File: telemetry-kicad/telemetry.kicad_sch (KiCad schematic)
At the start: 50 parts, among them J1 USB_C_Receptacle_USB2.0_16P, Q2 DMP3099LQ-7, SW1 SW_NRST, SW2 SW_BOOT0, U1 STM32H523RCT7, U2 AP2112K-3.3, U3 MAX-M10S-00B, U4 ASM330LHHXG1TR, U5 TCAN1044VDRQ1, U6 LMR33630ADDA, U7 USBLC6-2SC6, U8 TPS2116DRL

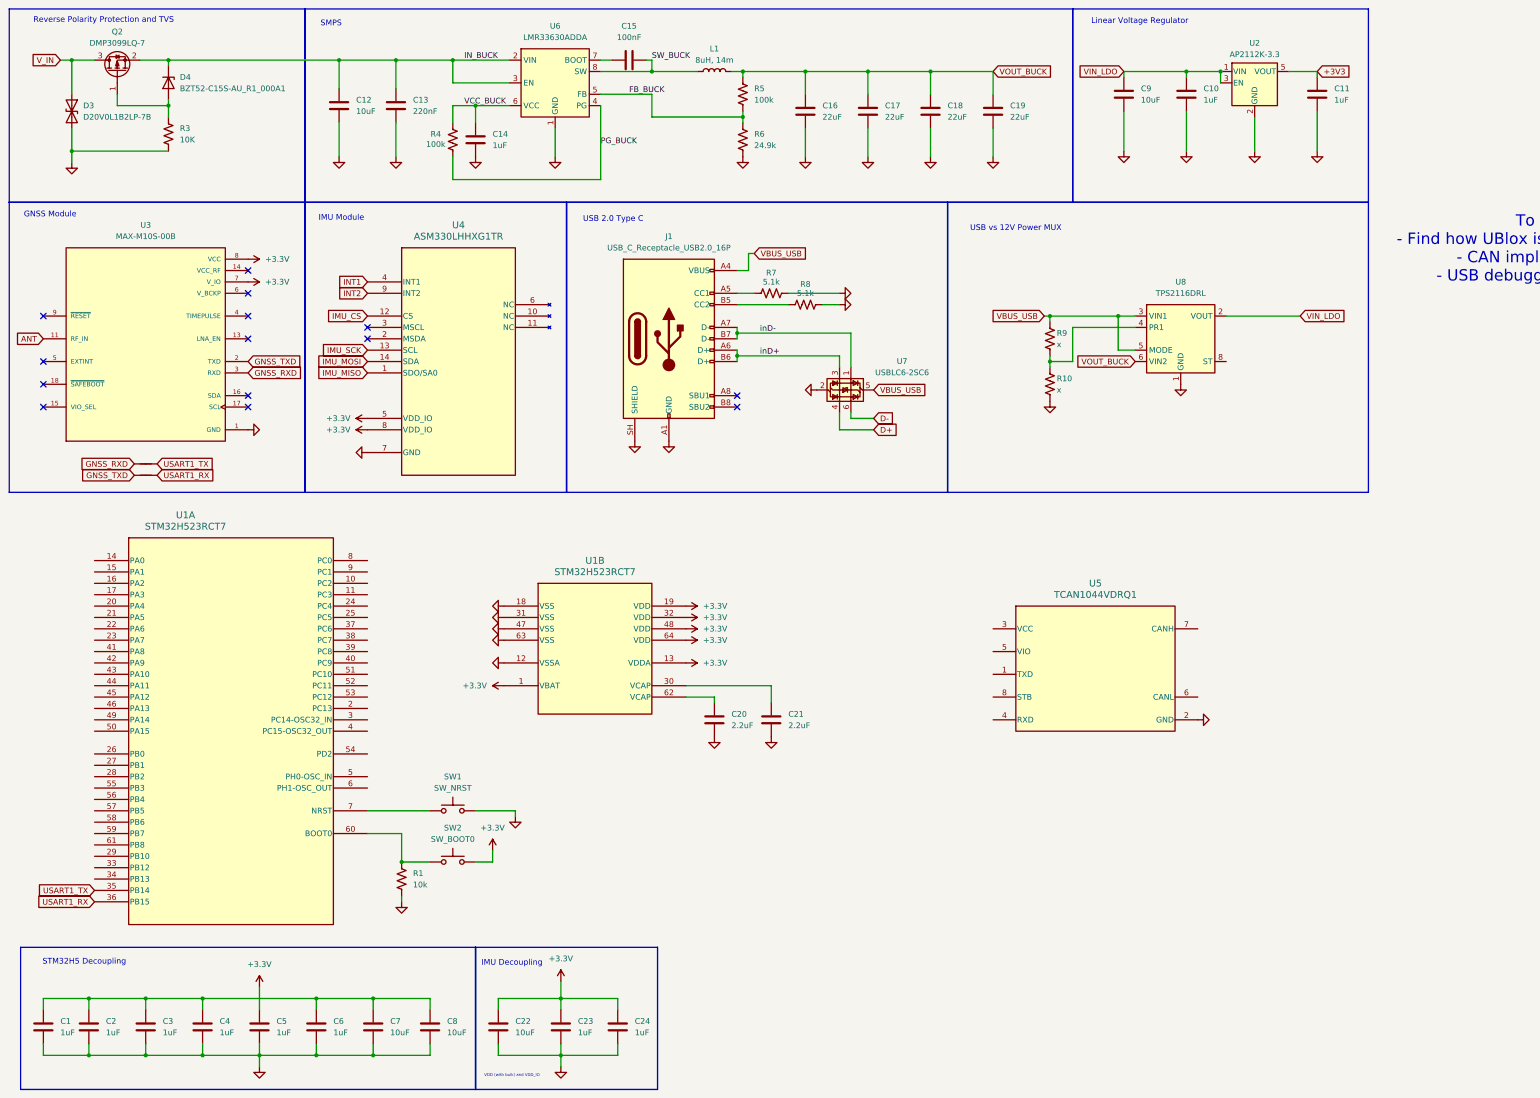
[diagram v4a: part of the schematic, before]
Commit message: Added flash and improved from suggestions. Power status flags go into MCU. Need to work on MCU Pin Plan and update documentation
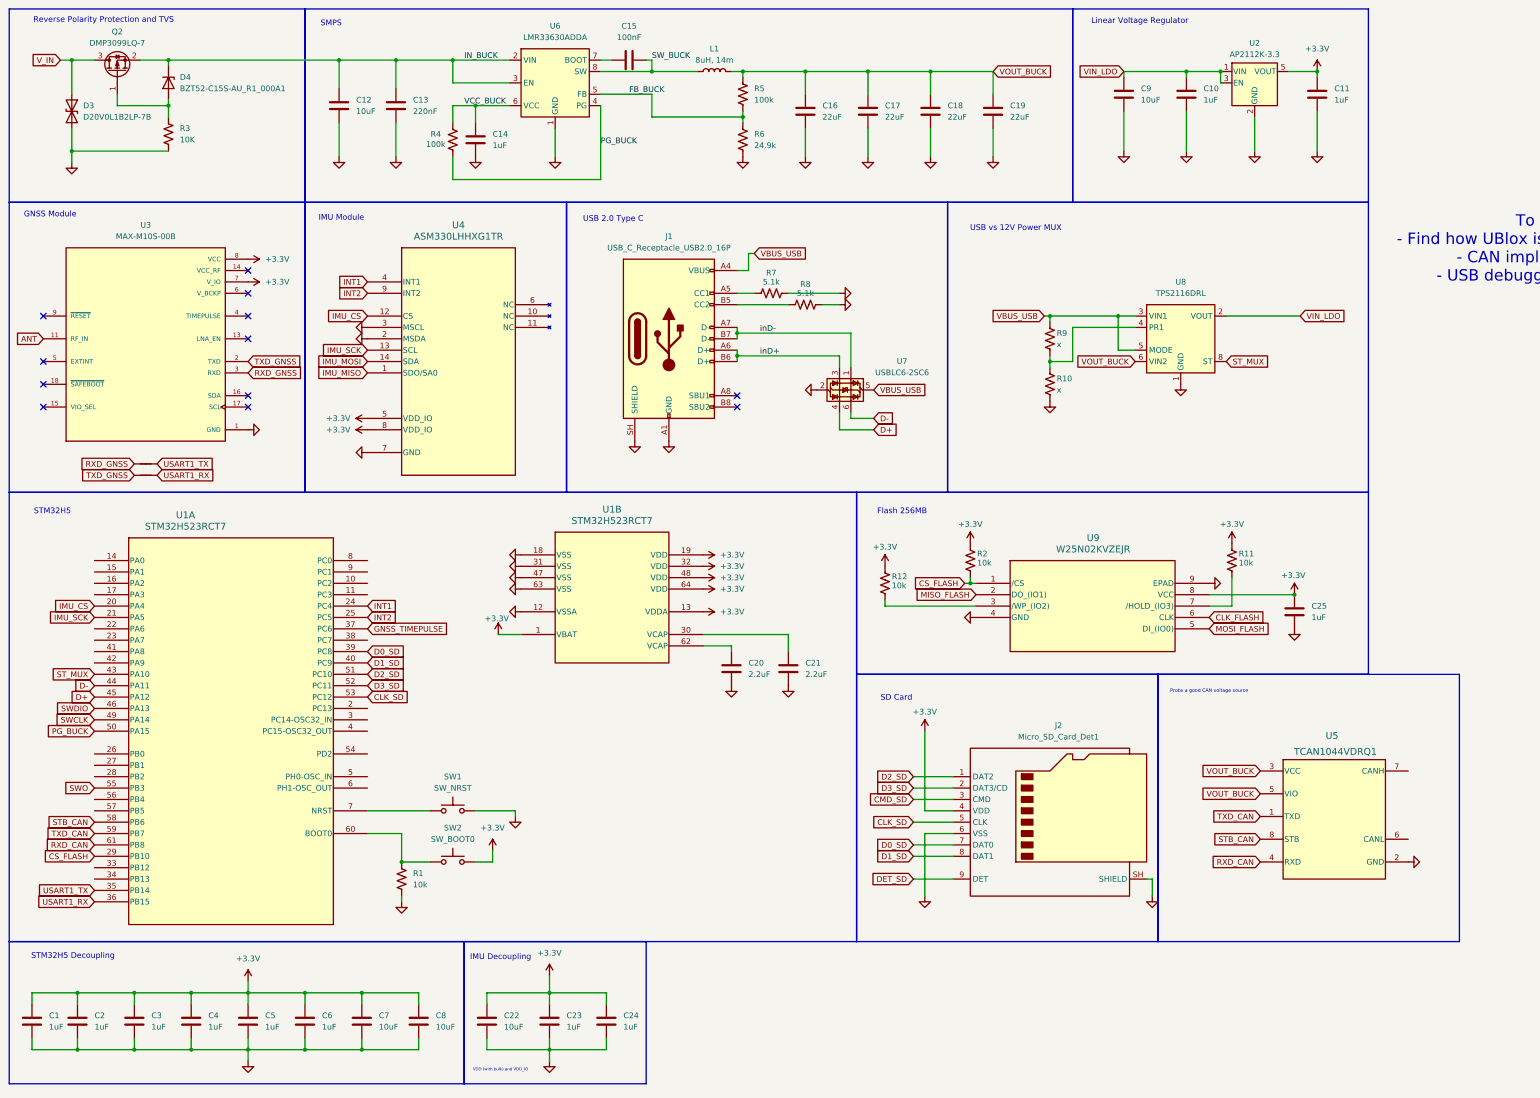
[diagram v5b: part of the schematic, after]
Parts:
- added C25: 1uF, symbol Device:C
- added J2: Micro_SD_Card_Det1, symbol Connector:Micro_SD_Card_Det1
- added R11, R12, R2: 10k, symbol Device:R_US
- added U9: W25N02KVZEJR, u-blox:W25N02KVZEJR, symbol telemetry:W25N02KVZEIR
- U5: footprint (none) -> D0008A-IPC_A
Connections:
- net +3V3 is gone; now on net +3.3V: C11.1, U2.5 (VOUT)
- net +3.3V: now also C1.1, C2.1, C3.1, C4.1, C6.1, C7.1, C8.1, C25.1, J2.4 (VDD), R11.1, R12.1, R2.1, U9.8 (VCC)
- net D+: now also U1.45 (PA12)
- net D-: now also U1.44 (PA11)
- net GND: now also U4.2 (MSDA), U4.3 (MSCL), C25.2, J2.6 (VSS), J2.SH (SHIELD), U9.4 (GND), U9.9 (EPAD)
- net IMU_CS: now also U1.20 (PA4)
- net IMU_SCK: now also U1.21 (PA5)
- net INT1: now also U1.24 (PC4)
- net INT2: now also U1.25 (PC5)
- net PG_BUCK: now also U1.50 (PA15)
- net VOUT_BUCK: now also U5.3 (VCC), U5.5 (VIO)
- net ST_MUX: now reaches U8.8 (ST)
- net ST_MUX: now also U1.43 (PA10)
- net CS_FLASH: now reaches U1.29 (PB10)
- net CS_FLASH: now also R2.2, U9.1 (/CS)
- net GNSS_TIMEPULSE: now reaches U1.37 (PC6)
- net D0_SD: now reaches U1.39 (PC8)
- net D0_SD: now also J2.7 (DAT0)
- net D1_SD: now reaches U1.40 (PC9)
- net D1_SD: now also J2.8 (DAT1)
- net SWDIO: now reaches U1.46 (PA13)
- net SWCLK: now reaches U1.49 (PA14)
- net D2_SD: now reaches U1.51 (PC10)
- net D2_SD: now also J2.1 (DAT2)
- net D3_SD: now reaches U1.52 (PC11)
- net D3_SD: now also J2.2 (DAT3/CD)
- net CLK_SD: now reaches U1.53 (PC12)
- net CLK_SD: now also J2.5 (CLK)
- net SWO: now reaches U1.55 (PB3)
- net STB_CAN: now reaches U1.58 (PB6)
- net STB_CAN: now also U5.8 (STB)
- net TXD_CAN: now reaches U1.59 (PB7)
- net TXD_CAN: now also U5.1 (TXD)
- net RXD_CAN: now reaches U1.61 (PB8)
- net RXD_CAN: now also U5.4 (RXD)
- net GNSS_RXD renamed RXD_GNSS
- net GNSS_TXD renamed TXD_GNSS
- new net: R12.2, U9.3 (/WP_(IO2))
- new net: R11.2, U9.7 (/HOLD_(IO3))
- new net CLK_FLASH: U9.6 (CLK)
- new net CMD_SD: J2.3 (CMD)
- new net DET_SD: J2.9 (DET)
- new net MISO_FLASH: U9.2 (DO_(IO1))
- new net MOSI_FLASH: U9.5 (DI_(IO0))
- no-connect marks 14 -> 12
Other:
- note added: "Flash 256MB"
- note added: "Probs a good CAN voltage source"
- note added: "SD Card"
- note added: "STM32H5"
- moved on the sheet: C1, C2, C20, C21, C22, C23, C24, C3, C4, C5, C6, C7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

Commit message: touch ups
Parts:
- removed C19: 22uF, Capacitor_SMD:C_0805_2012Metric_Pad1.18x1.45mm_HandSolder, symbol Device:C
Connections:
- net VOUT_BUCK is gone; now on net VIN_LDO: C16.1, C17.1, C18.1, L1.2, R5.1, U5.3 (VCC), U5.5 (VIO), U8.6 (VIN2)
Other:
- note added: "Fix net names"
- note added: "To do: - Find how UBlox is layed out on PCB - CAN terminal block - SMA connector for UBlox - HSE Crystal"
- note removed: "Probs a good CAN voltage source"
- note removed: "To do: - Find how UBlox is layed out on PCB - CAN implimentation - USB debugging and SWD"
- moved on the sheet: C10, C9

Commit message: Schematic wiring, CAN terminal block added and SMA connector added
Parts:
- added J3: 2601-1102, CONN2_2601-1102_WAG, symbol telemetry:2601-1102
- added J4: RFPC-SMA27-F, RFPC-SMA27-F:GRADCONN_RFPC-SMA27-F, symbol telemetry:RFPC-SMA27-F
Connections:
- net GNSS_TIMEPULSE is gone; now on net TIMEPULSE_GNSS: U1.37 (PC6)
- net IMU_MISO is gone; now on net MISO_IMU: U4.1 (SDO/SA0)
- net IMU_MOSI is gone; now on net MOSI_IMU: U4.14 (SDA)
- net CLK_FLASH: now also U1.27 (PB1)
- net CMD_SD: now also U1.54 (PD2)
- net MISO_FLASH: now also U1.26 (PB0)
- net MOSI_FLASH: now also U1.28 (PB2)
- net VIN_LDO: no longer C16.1, C17.1, C18.1, L1.2, R5.1, U5.3 (VCC), U5.5 (VIO), U8.6 (VIN2)
- net TIMEPULSE_GNSS: now reaches U3.4 (TIMEPULSE)
- net MISO_IMU: now reaches U1.22 (PA6)
- net MOSI_IMU: now reaches U1.23 (PA7)
- net at U5.6 (CANL): now also J3.3 (2_1), J3.4 (2_2)
- net at U5.7 (CANH): now also J3.1 (1_1), J3.2 (1_2)
- net IMU_CS renamed CS_IMU
- net IMU_SCK renamed SCK_IMU
- new net VOUT_BUCK: C16.1, C17.1, C18.1, L1.2, R5.1, U5.3 (VCC), U5.5 (VIO), U8.6 (VIN2)
- no-connect marks 12 -> 11
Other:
- note added: "GNSS Antenna Connector"
- note added: "To do: - Find how UBlox is layed out on PCB - Wire SMA connector - HSE Crystal - SD card series resistors - LEDs for debugging and power stages - NRST Cap"
- note removed: "Fix net names"
- note removed: "To do: - Find how UBlox is layed out on PCB - CAN terminal block - SMA connector for UBlox - HSE Crystal"
- moved on the sheet: C20, C21, J1, R10, R7, R8, R9, U4, U5, U7, U8

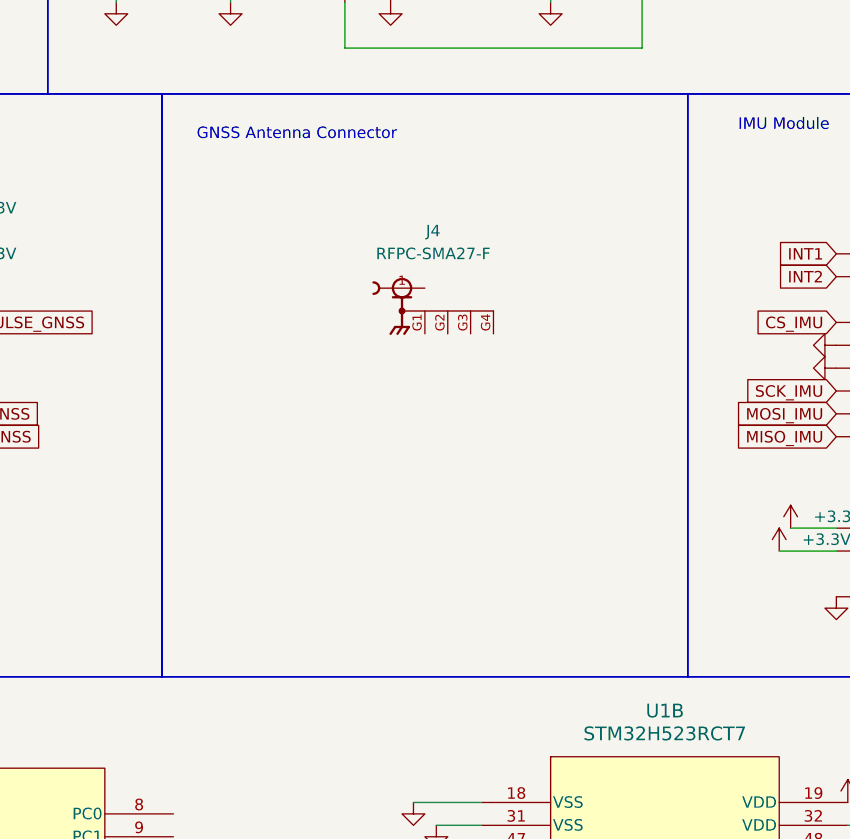
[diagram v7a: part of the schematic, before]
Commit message: HSE added
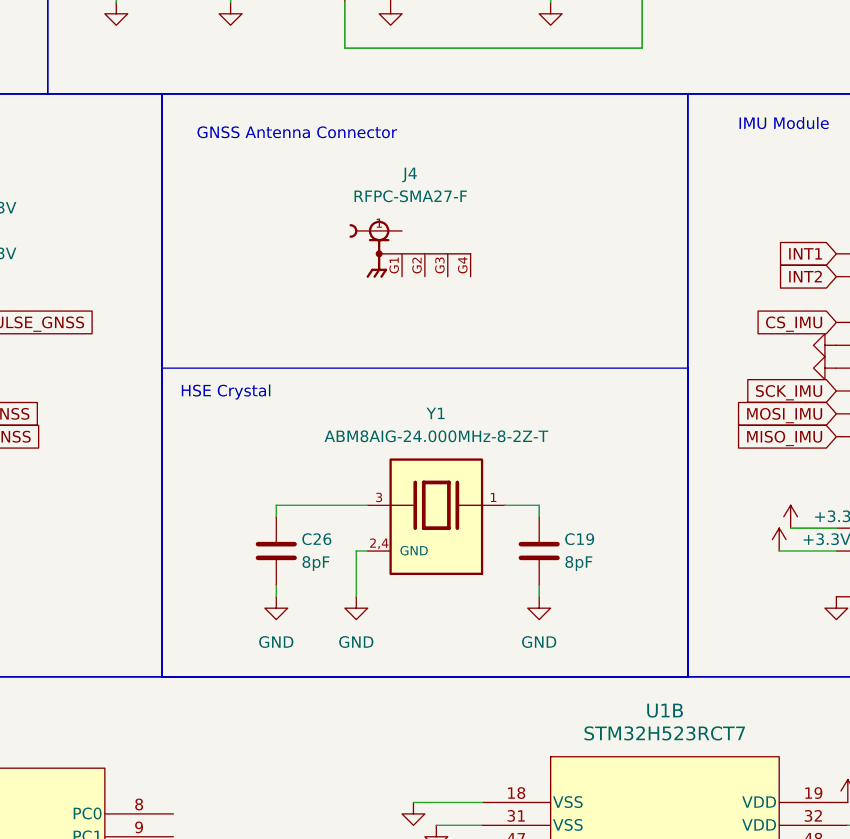
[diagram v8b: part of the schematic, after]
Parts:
- added C19, C26: 8pF, symbol Device:C
- added Y1: ABM8AIG-24.000MHz-8-2Z-T, ABM8AIG-24.000MHz-8-2Z-T:XTAL_ABM8AIG-24.000MHz-8-2Z-T, symbol telemetry:ABM8AIG-24.000MHz-8-2Z-T
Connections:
- net GND: now also C19.2, C26.2, Y1.2,4 (GND)
- new net: C19.1, Y1.1
- new net: C26.1, Y1.3
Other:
- note added: "HSE Crystal"
- moved on the sheet: J4
